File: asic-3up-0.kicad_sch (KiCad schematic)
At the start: 64 parts, among them J12 Conn_01x01, J13 Conn_01x01, J18 Conn_01x01, J3 Conn_01x01, J4 Conn_01x01, U28 MCP1824T-1202E/OT, U29 MCP1824T-1202E/OT, U30 MCP1824T-1202E/OT, U32 MCP1824T-0802E, U42 MCP1824T-0802E, U43 MCP1824T-0802E, U45 BM1362AC_MODE1, U46 BM1362AC_MODE0, U47 BM1362AC_MODE1

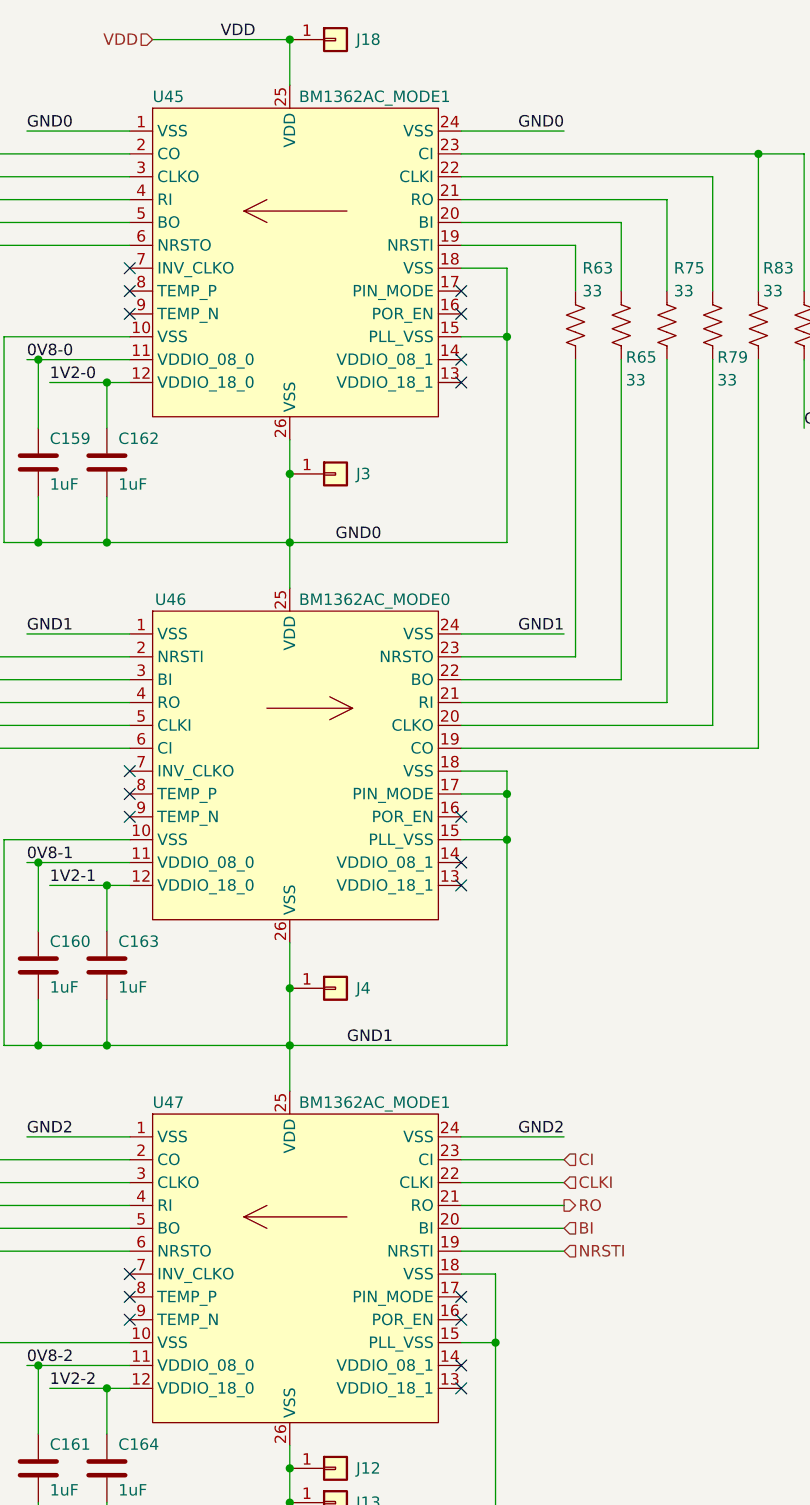
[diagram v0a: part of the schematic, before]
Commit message: fix PIN_MODE connections for #17
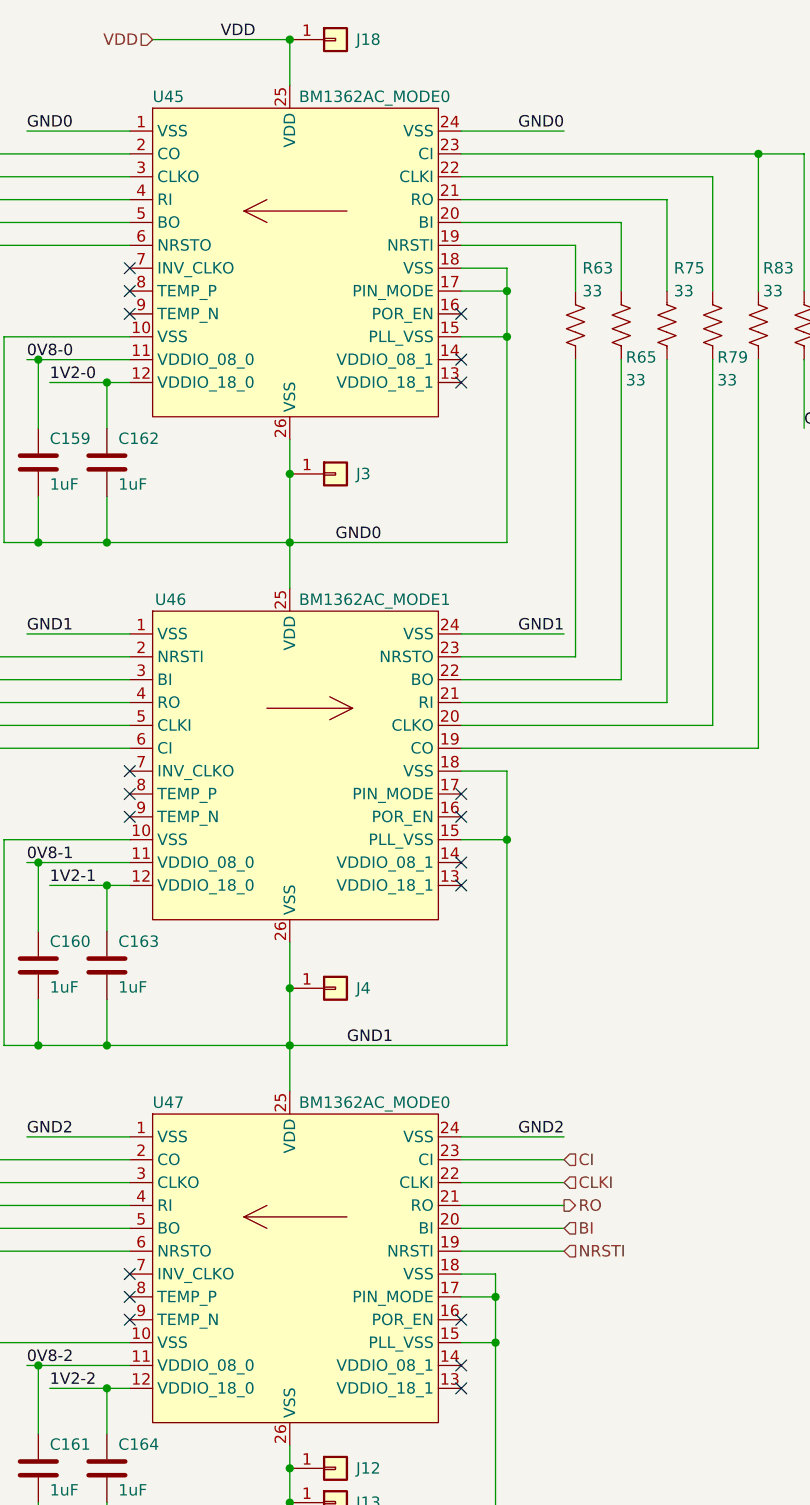
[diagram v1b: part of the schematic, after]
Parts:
- U45, U47: value BM1362AC_MODE1 -> BM1362AC_MODE0
- U46: value BM1362AC_MODE0 -> BM1362AC_MODE1
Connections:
- net GND0: now also U45.17 (PIN_MODE)
- net GND1: no longer U46.17 (PIN_MODE)
- net VSS: now also U47.17 (PIN_MODE)
- no-connect marks 26 -> 25
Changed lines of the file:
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@@
 	)
 	(junction
+		(at 250.19 120.65)
+		(diameter 0)
+		(color 0 0 0 0)
+	)
+	(junction
 		(at 198.12 240.03)
 		(diameter 0)
@@
 	)
 	(junction
-		(at 250.19 176.53)
-		(diameter 0)
-		(color 0 0 0 0)
-	)
-	(junction
 		(at 95.25 226.06)
 		(diameter 0.9144)
@@
 	)
 	(junction
+		(at 248.92 232.41)
+		(diameter 0)
+		(color 0 0 0 0)
+	)
+	(junction
 		(at 64.77 182.88)
 		(diameter 0.9144)
@@
 	)
 	(no_connect
-		(at 245.11 232.41)
-	)
-	(no_connect
 		(at 245.11 128.27)
 	)
@@
 	)
 	(no_connect
-		(at 245.11 120.65)
+		(at 208.28 179.07)
 	)
 	(no_connect
-		(at 208.28 179.07)
+		(at 245.11 176.53)
 	)
 	(no_connect
@@
 	(wire
 		(pts
+			(xy 248.92 232.41) (xy 248.92 237.49)
+		)
+		(stroke
+			(width 0)
+			(type default)
+		)
+	)
+	(wire
+		(pts
 			(xy 34.29 179.07) (xy 34.29 182.88)
 		)
@@
 	(wire
 		(pts
+			(xy 250.19 120.65) (xy 250.19 118.11)
+		)
+		(stroke
+			(width 0)
+			(type default)
+		)
+	)
+	(wire
+		(pts
 			(xy 323.85 170.18) (xy 323.85 172.72)
 		)
@@
 	(wire
 		(pts
-			(xy 250.19 176.53) (xy 250.19 173.99)
-		)
-		(stroke
-			(width 0)
-			(type default)
-		)
-	)
-	(wire
-		(pts
 			(xy 283.21 105.41) (xy 278.13 105.41)
 		)
@@
 	(wire
 		(pts
-			(xy 250.19 181.61) (xy 250.19 176.53)
+			(xy 250.19 173.99) (xy 250.19 181.61)
+		)
+		(stroke
+			(width 0)
+			(type default)
+		)
+	)
+	(wire
+		(pts
+			(xy 245.11 232.41) (xy 248.92 232.41)
 		)
 		(stroke
@@
 	(wire
 		(pts
-			(xy 245.11 176.53) (xy 250.19 176.53)
-		)
-		(stroke
-			(width 0)
-			(type default)
-		)
-	)
-	(wire
-		(pts
 			(xy 205.74 130.81) (xy 208.28 130.81)
 		)
@@
 	(wire
 		(pts
-			(xy 248.92 229.87) (xy 248.92 237.49)
+			(xy 248.92 229.87) (xy 248.92 232.41)
 		)
 		(stroke
@@
 	(wire
 		(pts
-			(xy 250.19 125.73) (xy 250.19 118.11)
+			(xy 250.19 125.73) (xy 250.19 120.65)
 		)
 		(stroke
@@
 	(wire
 		(pts
+			(xy 245.11 120.65) (xy 250.19 120.65)
+		)
+		(stroke
+			(width 0)
+			(type default)
+		)
+	)
+	(wire
+		(pts
 			(xy 273.05 168.91) (xy 245.11 168.91)
 		)
@@
 			)
 		)
-		(property "Value" "BM1362AC_MODE1"
+		(property "Value" "BM1362AC_MODE0"
 			(at 227.076 99.06 0)
 			(effects
@@
 			)
 		)
-		(property "Value" "BM1362AC_MODE0"
+		(property "Value" "BM1362AC_MODE1"
 			(at 227.076 154.94 0)
 			(effects
@@
 			)
 		)
-		(property "Value" "BM1362AC_MODE1"
+		(property "Value" "BM1362AC_MODE0"
 			(at 227.076 210.82 0)
 			(effects

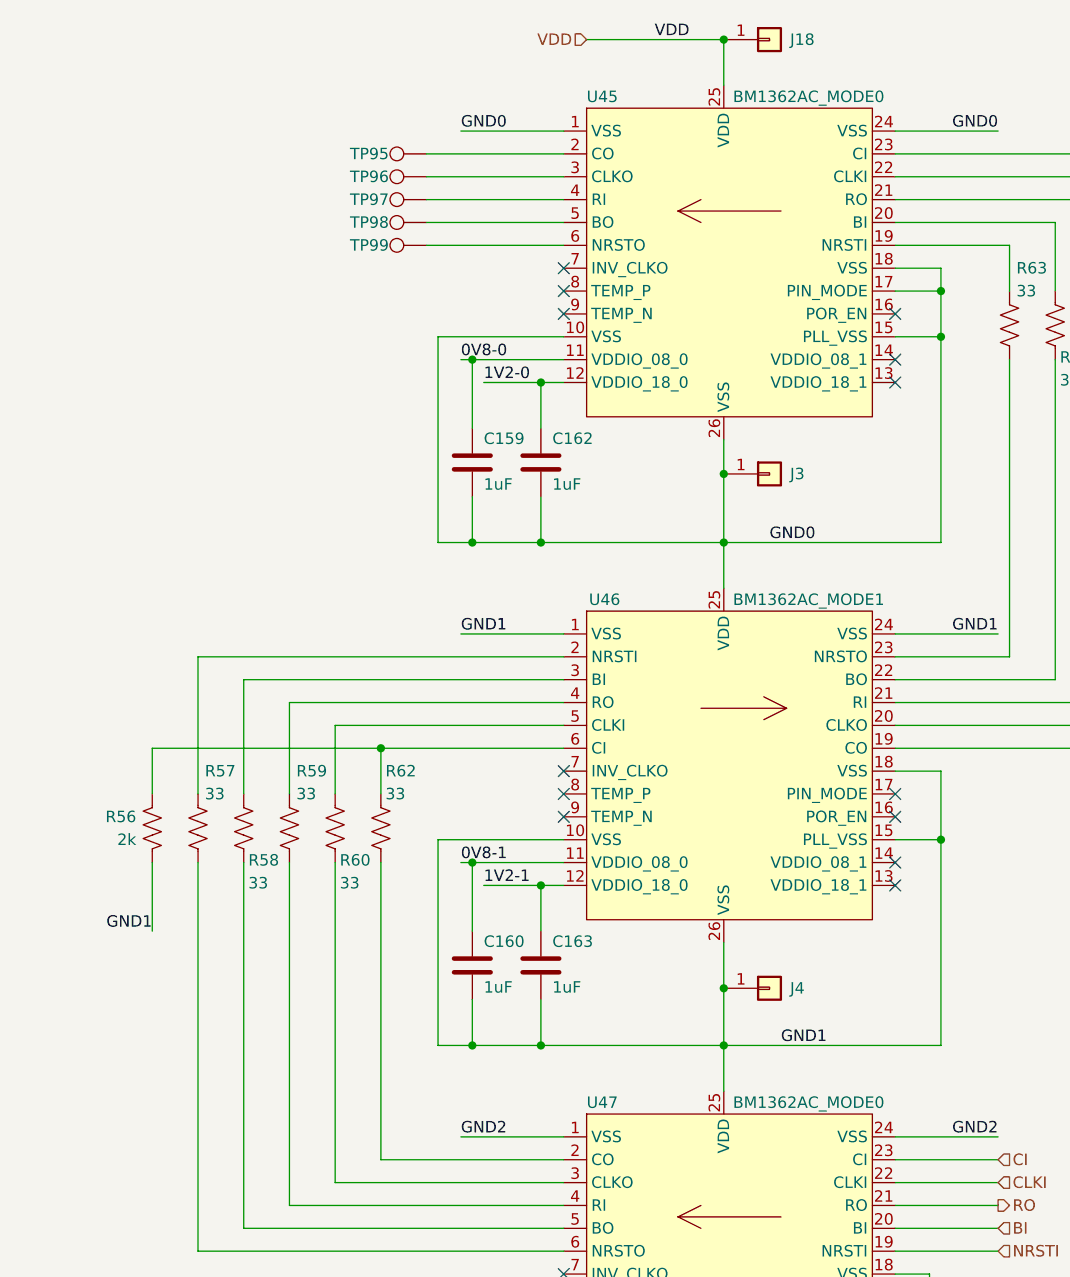
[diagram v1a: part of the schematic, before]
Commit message: added RI pullup resistors for #16. updated BOM. bumped version number to 3
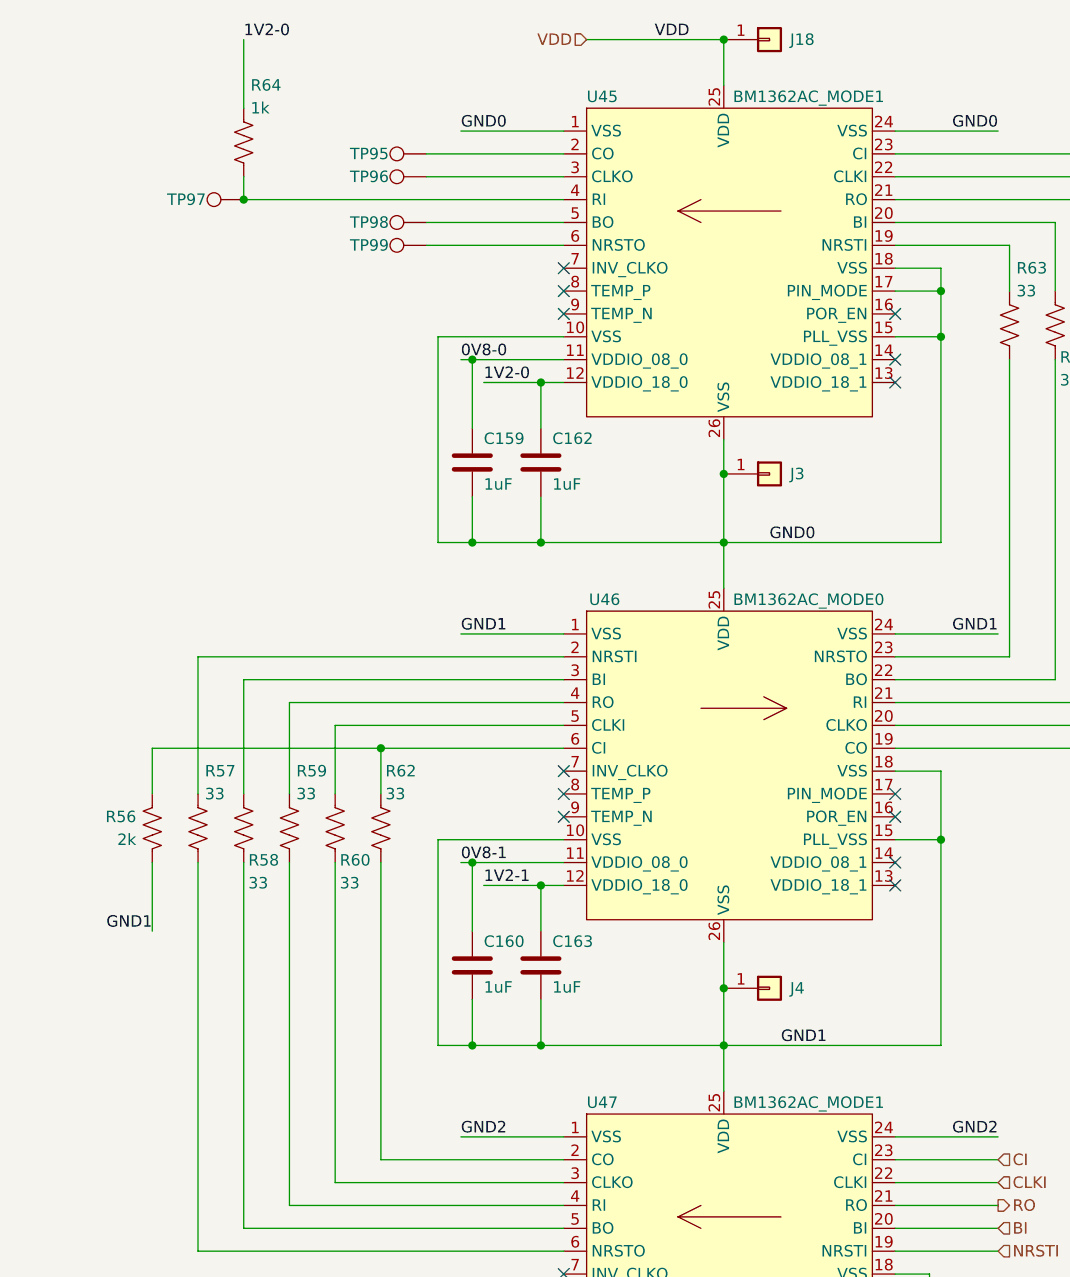
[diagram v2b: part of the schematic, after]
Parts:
- added R64: 1k, Resistor_SMD:R_0402_1005Metric, symbol Device:R_US
- U45, U47: value BM1362AC_MODE0 -> BM1362AC_MODE1
- U46: value BM1362AC_MODE1 -> BM1362AC_MODE0
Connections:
- net 1V2-0: now also R64.1
- net at TP97.1, U45.4 (RI): now also R64.2
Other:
- title: (none) -> emberOne/00
- moved on the sheet: TP97
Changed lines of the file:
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@@
 	(paper "A3")
 	(title_block
-		(date "2024-11-25")
-		(rev "2")
+		(title "emberOne/00")
+		(date "2025-02-25")
+		(rev "3")
 	)
 	(text "Reference Voltage Regulators"
@@
 	)
 	(junction
+		(at 172.72 110.49)
+		(diameter 0)
+		(color 0 0 0 0)
+	)
+	(junction
 		(at 226.06 204.47)
 		(diameter 0)
@@
 	(wire
 		(pts
-			(xy 193.04 110.49) (xy 208.28 110.49)
-		)
-		(stroke
-			(width 0)
-			(type default)
-		)
-	)
-	(wire
-		(pts
 			(xy 68.58 226.06) (xy 68.58 228.6)
 		)
@@
 	(wire
 		(pts
+			(xy 172.72 110.49) (xy 172.72 107.95)
+		)
+		(stroke
+			(width 0)
+			(type default)
+		)
+	)
+	(wire
+		(pts
 			(xy 64.77 171.45) (xy 63.5 171.45)
 		)
@@
 	(wire
 		(pts
+			(xy 172.72 110.49) (xy 208.28 110.49)
+		)
+		(stroke
+			(width 0)
+			(type default)
+		)
+	)
+	(wire
+		(pts
 			(xy 101.6 171.45) (xy 101.6 168.91)
 		)
@@
 	(wire
 		(pts
+			(xy 172.72 92.71) (xy 172.72 100.33)
+		)
+		(stroke
+			(width 0)
+			(type default)
+		)
+	)
+	(wire
+		(pts
 			(xy 41.91 113.03) (xy 43.18 113.03)
 		)
@@
 		)
 	)
+	(label "1V2-0"
+		(at 172.72 92.71 0)
+		(effects
+			(font
+				(size 1.27 1.27)
+			)
+			(justify left bottom)
+		)
+	)
 	(label "VDD"
 		(at 222.25 92.71 180)
@@
 			)
 		)
-		(property "Value" "BM1362AC_MODE0"
+		(property "Value" "BM1362AC_MODE1"
 			(at 227.076 99.06 0)
 			(effects
@@
 	(symbol
 		(lib_id "Connector:TestPoint")
-		(at 193.04 110.49 90)
+		(at 172.72 110.49 90)
 		(mirror x)
 		(unit 1)
@@
 		(dnp no)
 		(property "Reference" "TP97"
-			(at 186.69 110.49 90)
+			(at 166.37 110.49 90)
 			(effects
 				(font
@@
 		)
 		(property "Value" "TestPoint"
-			(at 187.325 111.7599 90)
+			(at 167.005 111.7599 90)
 			(effects
 				(font
@@
 		)
 		(property "Footprint" "TestPoint:TestPoint_Pad_D1.0mm"
-			(at 193.04 115.57 0)
+			(at 172.72 115.57 0)
 			(effects
 				(font
@@
 		)
 		(property "Datasheet" "~"
-			(at 193.04 115.57 0)
+			(at 172.72 115.57 0)
 			(effects
 				(font
@@
 		)
 		(property "Description" ""
-			(at 193.04 110.49 0)
+			(at 172.72 110.49 0)
 			(effects
 				(font
@@
 	)
 	(symbol
+		(lib_id "Device:R_US")
+		(at 172.72 104.14 0)
+		(unit 1)
+		(exclude_from_sim no)
+		(in_bom yes)
+		(on_board yes)
+		(dnp no)
+		(property "Reference" "R64"
+			(at 173.482 97.79 0)
+			(effects
+				(font
+					(size 1.27 1.27)
+				)
+				(justify left)
+			)
+		)
+		(property "Value" "1k"
+			(at 173.482 100.33 0)
+			(effects
+				(font
+					(size 1.27 1.27)
+				)
+				(justify left)
+			)
+		)
+		(property "Footprint" "Resistor_SMD:R_0402_1005Metric"
+			(at 173.736 104.394 90)
+			(effects
+				(font
+					(size 1.27 1.27)
+				)
+				(hide yes)
+			)
+		)
+		(property "Datasheet" "~"
+			(at 172.72 104.14 0)
+			(effects
+				(font
+					(size 1.27 1.27)
+				)
+				(hide yes)
+			)
+		)
+		(property "Description" "Resistor, US symbol"
+			(at 172.72 104.14 0)
+			(effects
+				(font
+					(size 1.27 1.27)
+				)
+				(hide yes)
+			)
+		)
+		(property "DK" "311-1.00KLRCT-ND"
+			(at 172.72 104.14 0)
+			(effects
+				(font
+					(size 1.27 1.27)
+				)
+				(hide yes)
+			)
+		)
+		(property "PARTNO" "RC0402FR-072KL"
+			(at 172.72 104.14 0)
+			(effects
+				(font
+					(size 1.27 1.27)
+				)
+				(hide yes)
+			)
+		)
+		(pin "1"
+		)
+		(pin "2"
+		)
+		(instances
+			(project "emberone"
+				(path "/b036224c-4cdf-48cc-81df-19bc5283ebd2/dea5684e-9ec9-4967-b9ef-d4ee852a3fa0"
+					(reference "R64")
+					(unit 1)
+				)
+			)
+		)
+	)
+	(symbol
 		(lib_id "Device:C")
 		(at 198.12 139.7 0)
@@
 			)
 		)
-		(property "Value" "BM1362AC_MODE1"
+		(property "Value" "BM1362AC_MODE0"
 			(at 227.076 154.94 0)
 			(effects
@@
 			)
 		)
-		(property "Value" "BM1362AC_MODE0"
+		(property "Value" "BM1362AC_MODE1"
 			(at 227.076 210.82 0)
 			(effects
